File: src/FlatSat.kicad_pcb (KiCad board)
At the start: 2 copper layers, 48 x 32 mm, 37 parts, among them J1 LiPo, J2 Conn_01x04_MountingPin, J3 Conn_01x04_MountingPin, J4 Conn_02x03_Odd_Even, J5 Conn_01x12_Pin, J7 Micro_SD_Card_Det2, U1 Xiao, U2 MPU-6050 / 6500, U3 BME280 /BMP280, U4 MiniMeter

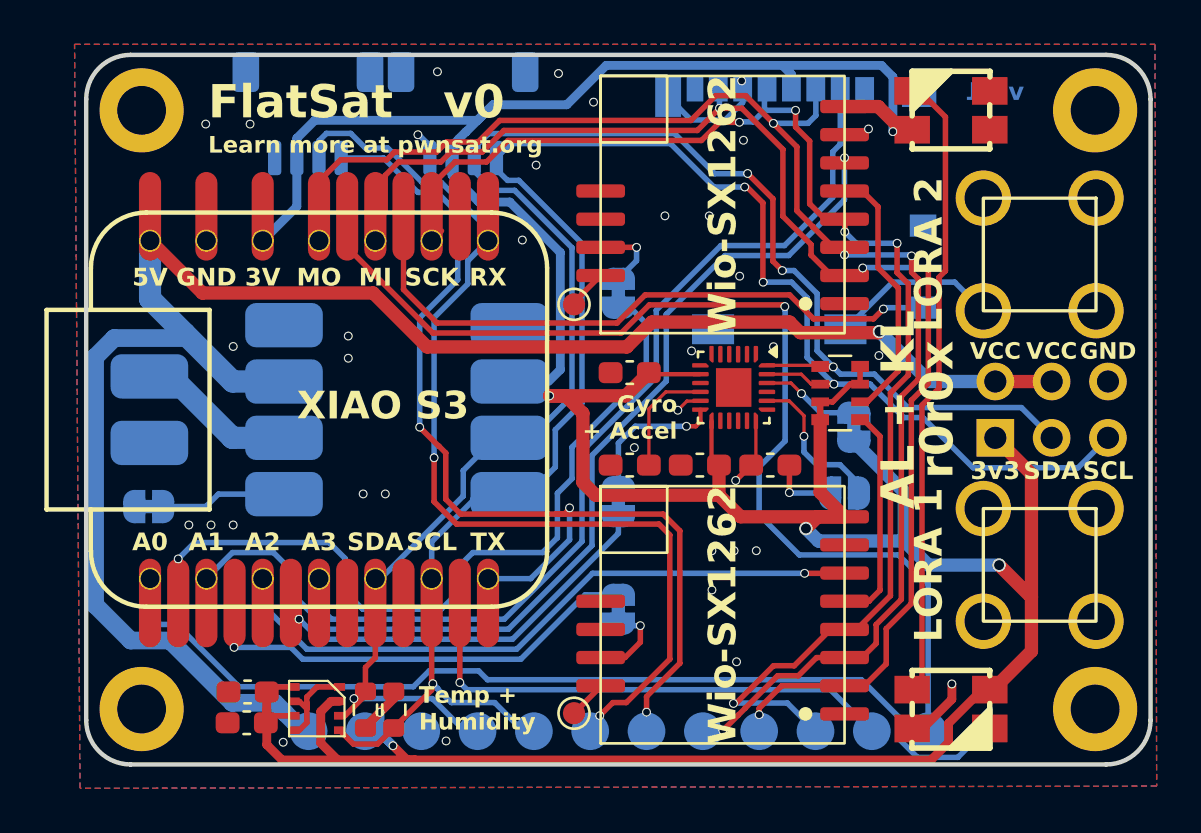
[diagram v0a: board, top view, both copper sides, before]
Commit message: update routing for MPU6050 + fix traces + jumpers
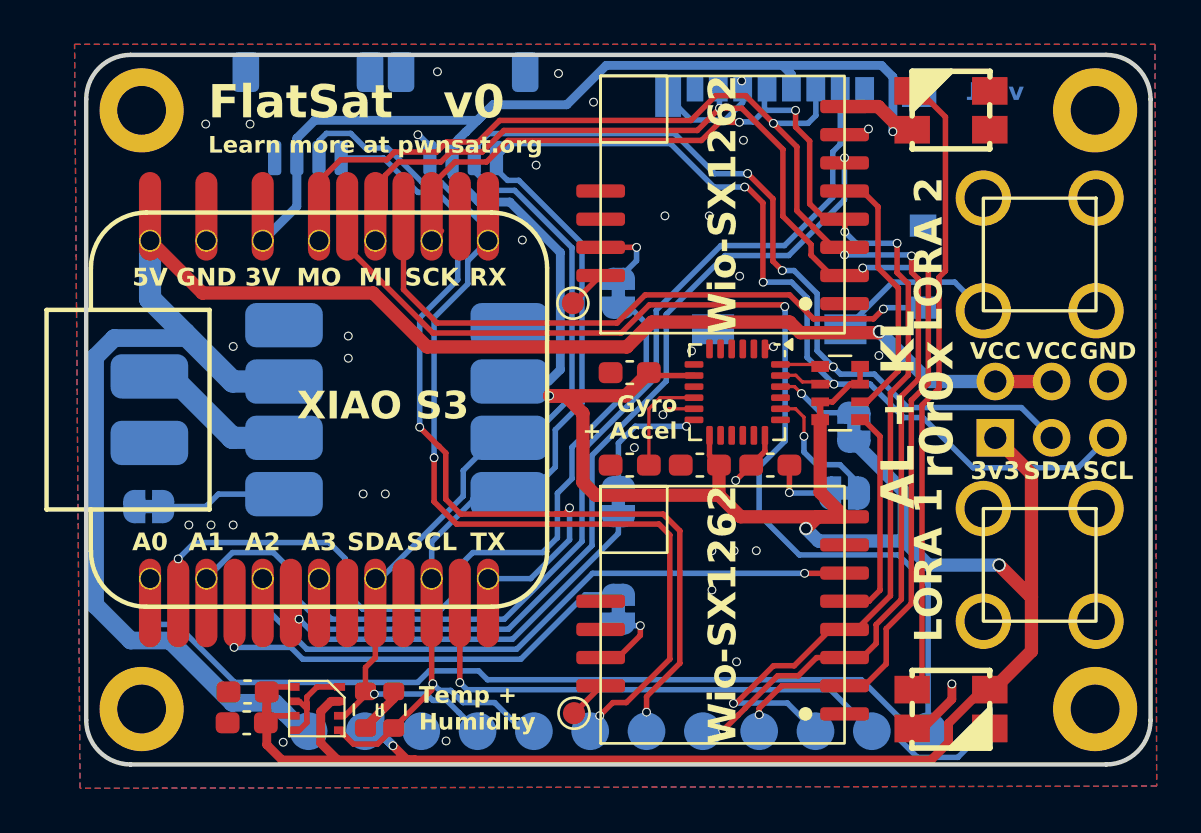
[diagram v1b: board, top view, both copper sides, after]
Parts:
- JP4: value SolderJumper_2_Open -> SolderJumper_2_Bridged; footprint Jumper:SolderJumper-2_P1.3mm_Open_RoundedPad1.0x1.5mm -> Jumper:SolderJumper-2_P1.3mm_Bridged_RoundedPad1.0x1.5mm
- U2: footprint Package_DFN_QFN:QFN-24-1EP_3x3mm_P0.4mm_EP1.75x1.6mm -> Sensor_Motion:InvenSense_QFN-24_4x4mm_P0.5mm
- moved U2 0.26 mm to (5.36, -0.79)
- moved TP1 0.07 mm to (-2.05, -4.80)
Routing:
- net SDA: track 79.3 -> 77.3 mm
- net Net-(JP2-A): track 6.63 -> 5.37 mm
- net +3V3: track 177.7 -> 176.9 mm
- net Net-(JP4-A): track 7.08 -> 6.28 mm
- net GND: track 25.4 -> 26.1 mm
- net NCS: track 4.48 -> 3.80 mm
- net SCL: track 83.4 -> 82.8 mm
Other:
- board text added: "Fonts Used: - Alkheimal - Atemica Sans - Glock Grotesque - Space Grotesk - Montserrat (I need to use less fonts)"
- board text added: "MPU6050 (will be deprecated) - 4x4mm MPU6500 () - 3x3mm - Disconnect JP4"

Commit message: update v0.2 gerber + pnp file
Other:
- board text added: "v0.2"
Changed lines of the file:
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@@
 		(layer "Edge.Cuts")
 	)
-	(gr_text "v0.1"
+	(gr_text "v0.2"
 		(at 18.3 -13.87 0)
 		(layer "B.Cu")
@@
 			(justify left bottom mirror)
 		)
-		(render_cache "v0.1" 0
+		(render_cache "v0.2" 0
 			(polygon
 				(pts
@@
 			(polygon
 				(pts
-					(xy 16.441311 -14.006) (xy 16.441311 -14.722657) (xy 16.362714 -14.643571) (xy 16.59792 -14.643571)
-					(xy 16.59792 -14.789433) (xy 16.259595 -14.789433) (xy 16.259595 -14.006)
+					(xy 16.539888 -14.006) (xy 16.539888 -14.123041) (xy 16.237124 -14.408561) (xy 16.205064 -14.441514)
+					(xy 16.184905 -14.467179) (xy 16.170016 -14.492595) (xy 16.161849 -14.513829) (xy 16.155987 -14.553836)
+					(xy 16.159699 -14.582982) (xy 16.170208 -14.606416) (xy 16.187543 -14.625497) (xy 16.210014 -14.638973)
+					(xy 16.240307 -14.647874) (xy 16.280746 -14.651191) (xy 16.32934 -14.646217) (xy 16.372777 -14.631701)
+					(xy 16.411004 -14.607351) (xy 16.443265 -14.57235) (xy 16.574961 -14.657102) (xy 16.54184 -14.698155)
+					(xy 16.500572 -14.73351) (xy 16.450104 -14.763397) (xy 16.395251 -14.784738) (xy 16.333672 -14.798002)
+					(xy 16.264187 -14.802622) (xy 16.206383 -14.799261) (xy 16.155698 -14.789682) (xy 16.111144 -14.774436)
+					(xy 16.069851 -14.752466) (xy 16.036256 -14.72584) (xy 16.009392 -14.694422) (xy 15.989512 -14.658389)
+					(xy 15.977359 -14.617849) (xy 15.973147 -14.571715) (xy 15.975599 -14.533857) (xy 15.983014 -14.495951)
+					(xy 15.996853 -14.458573) (xy 16.021263 -14.416572) (xy 16.054157 -14.374943) (xy 16.104745 -14.323466)
+					(xy 16.355191 -14.087967) (xy 16.38919 -14.154108) (xy 15.94711 -14.154108) (xy 15.94711 -14.006)
 				)
 			)
@@
 	)
 	(segment
-		(start -20.22 10.41)
-		(end -22 10.41)
-		(width 0.8)
-		(layer "B.Cu")
-		(net 17)
-	)
-	(segment
 		(start -19.5425 -3.4175)
 		(end -21.12 -4.995)
@@
 	)
 	(segment
-		(start -15.041 13.669)
-		(end -15.49 13.22)
-		(width 0.8)
-		(layer "B.Cu")
-		(net 17)
-	)
-	(segment
-		(start -19.355 -3.23)
-		(end -19.5425 -3.4175)
+		(start -23.599 8.811)
+		(end -23.599 -2.365322)
 		(width 0.8)
 		(layer "B.Cu")
@@
 	)
 	(segment
-		(start -14.569 14.141)
-		(end -14.569 14.138214)
+		(start -22 10.41)
+		(end -23.599 8.811)
 		(width 0.8)
 		(layer "B.Cu")
@@
 	)
 	(segment
-		(start -15.038214 13.669)
-		(end -15.041 13.669)
+		(start -15.041 13.669)
+		(end -15.49 13.22)
 		(width 0.8)
 		(layer "B.Cu")
@@
 	)
 	(segment
-		(start -14.569 14.138214)
-		(end -15.038214 13.669)
+		(start -14.21 14.5)
+		(end -14.569 14.141)
 		(width 0.8)
 		(layer "B.Cu")
@@
 	)
 	(segment
-		(start -13.97 14.5)
-		(end -14.21 14.5)
+		(start -15.038214 13.669)
+		(end -15.041 13.669)
 		(width 0.8)
 		(layer "B.Cu")
@@
 	)
 	(segment
-		(start 17 -1.27)
-		(end 14.022 -1.27)
-		(width 0.6)
+		(start -22.734322 -3.23)
+		(end -19.355 -3.23)
+		(width 0.8)
 		(layer "B.Cu")
 		(net 17)
 	)
 	(segment
-		(start -22 10.41)
-		(end -23.599 8.811)
+		(start -17.41 13.22)
+		(end -20.22 10.41)
 		(width 0.8)
 		(layer "B.Cu")
@@
 	)
 	(segment
-		(start -23.599 8.811)
-		(end -23.599 -2.365322)
+		(start -14.569 14.138214)
+		(end -15.038214 13.669)
 		(width 0.8)
 		(layer "B.Cu")
@@
 	)
 	(segment
-		(start -22.734322 -3.23)
-		(end -19.355 -3.23)
-		(width 0.8)
+		(start 17 -1.27)
+		(end 14.022 -1.27)
+		(width 0.6)
 		(layer "B.Cu")
 		(net 17)
@@
 	)
 	(segment
-		(start -17.41 13.22)
-		(end -20.22 10.41)
+		(start -13.97 14.5)
+		(end -14.21 14.5)
 		(width 0.8)
 		(layer "B.Cu")
@@
 	)
 	(segment
+		(start -20.22 10.41)
+		(end -22 10.41)
+		(width 0.8)
+		(layer "B.Cu")
+		(net 17)
+	)
+	(segment
 		(start -21.12 -4.995)
 		(end -21.12 -7.62)
@@
 	)
 	(segment
+		(start -19.355 -3.23)
+		(end -19.5425 -3.4175)
+		(width 0.8)
+		(layer "B.Cu")
+		(net 17)
+	)
+	(segment
 		(start -19.5425 -3.4175)
 		(end -17.395 -1.27)
@@
 	)
 	(segment
-		(start -14.21 14.5)
-		(end -14.569 14.141)
+		(start -14.569 14.141)
+		(end -14.569 14.138214)
 		(width 0.8)
 		(layer "B.Cu")
